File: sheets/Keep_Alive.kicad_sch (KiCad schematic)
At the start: 7 parts, among them IC1 PSM712-LF-T7, U41 MIC5205-3.3YM5

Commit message: Remediate power supply, main relay keep-alive, and schematic ERC to 0 errors
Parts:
- added D20, D21: B340A-13-F, Diode_SMD:D_SMA, symbol Device:D_Schottky
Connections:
- new net 12V_IGN_SW: D20.2 (A)
- new net 12V_MR: D21.2 (A)
- new net 12V_RAW: D20.1 (K), D21.1 (K)
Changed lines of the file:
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@@
+		)
+	)
+	(hierarchical_label "12V_IGN_SW"
+		(shape input)
+		(at 67.31 45.72 180)
+		(fields_autoplaced yes)
+		(effects (font (size 1.27 1.27)) (justify right))
+	)
+	(hierarchical_label "12V_MR"
+		(shape input)
+		(at 67.31 55.88 180)
+		(fields_autoplaced yes)
+		(effects (font (size 1.27 1.27)) (justify right))
+	)
+	(hierarchical_label "12V_RAW"
+		(shape output)
+		(at 120.65 45.72 0)
+		(fields_autoplaced yes)
+		(effects (font (size 1.27 1.27)) (justify left))
+	)
+	(wire
+		(pts (xy 67.31 45.72) (xy 86.36 45.72))
+		(stroke (width 0) (type default))
+	)
+	(wire
+		(pts (xy 67.31 55.88) (xy 86.36 55.88))
+		(stroke (width 0) (type default))
+	)
+	(wire
+		(pts (xy 93.98 45.72) (xy 105.41 45.72))
+		(stroke (width 0) (type default))
+	)
+	(wire
+		(pts (xy 93.98 55.88) (xy 105.41 55.88))
+		(stroke (width 0) (type default))
+	)
+	(wire
+		(pts (xy 105.41 55.88) (xy 105.41 45.72))
+		(stroke (width 0) (type default))
+	)
+	(wire
+		(pts (xy 105.41 45.72) (xy 120.65 45.72))
+		(stroke (width 0) (type default))
+	)
+	(junction
+		(at 105.41 45.72)
+		(diameter 0)
+		(color 0 0 0 0)
+	)
+	(symbol
+		(lib_id "Device:D_Schottky")
+		(at 90.17 45.72 180)
+		(unit 1)
+		(exclude_from_sim no)
+		(in_bom yes)
+		(on_board yes)
+		(dnp no)
+		(property "Reference" "D20"
+			(at 90.17 43.18 0)
+			(effects (font (size 1.27 1.27)))
+		)
+		(property "Value" "B340A-13-F"
+			(at 90.17 48.26 0)
+			(effects (font (size 1.27 1.27)))
+		)
+		(property "Footprint" "Diode_SMD:D_SMA"
+			(at 90.17 45.72 0)
+			(effects (font (size 1.27 1.27)) (hide yes))
+		)
+		(property "Datasheet" "~"
+			(at 90.17 45.72 0)
+			(effects (font (size 1.27 1.27)) (hide yes))
+		)
+		(property "Description" "40V 3A Schottky Barrier Diode (IGN_SW -> 12V_RAW OR-ing)"
+			(at 90.17 45.72 0)
+			(effects (font (size 1.27 1.27)) (hide yes))
+		)
+		(property "LCSC" "C8598"
+			(at 90.17 45.72 0)
+			(effects (font (size 1.27 1.27)) (hide yes))
+		)
+		(pin "1")
+		(pin "2")
+		(instances
+			(project "fome-mc"
+				(path "/3b9c5ffd-e59b-402d-8c5e-052f7ca643a4/46495fed-359e-4c30-808a-9217af090de7"
+					(reference "D20")
+					(unit 1)
+				)
+			)
+		)
+	)
+	(symbol
+		(lib_id "Device:D_Schottky")
+		(at 90.17 55.88 180)
+		(unit 1)
+		(exclude_from_sim no)
+		(in_bom yes)
+		(on_board yes)
+		(dnp no)
+		(property "Reference" "D21"
+			(at 90.17 53.34 0)
+			(effects (font (size 1.27 1.27)))
+		)
+		(property "Value" "B340A-13-F"
+			(at 90.17 58.42 0)
+			(effects (font (size 1.27 1.27)))
+		)
+		(property "Footprint" "Diode_SMD:D_SMA"
+			(at 90.17 55.88 0)
+			(effects (font (size 1.27 1.27)) (hide yes))
+		)
+		(property "Datasheet" "~"
+			(at 90.17 55.88 0)
+			(effects (font (size 1.27 1.27)) (hide yes))
+		)
+		(property "Description" "40V 3A Schottky Barrier Diode (12V_MR -> 12V_RAW Keep-Alive OR-ing)"
+			(at 90.17 55.88 0)
+			(effects (font (size 1.27 1.27)) (hide yes))
+		)
+		(property "LCSC" "C8598"
+			(at 90.17 55.88 0)
+			(effects (font (size 1.27 1.27)) (hide yes))
+		)
+		(pin "1")
+		(pin "2")
+		(instances
+			(project "fome-mc"
+				(path "/3b9c5ffd-e59b-402d-8c5e-052f7ca643a4/46495fed-359e-4c30-808a-9217af090de7"
+					(reference "D21")
+					(unit 1)
+				)
+			)
 		)
 	)

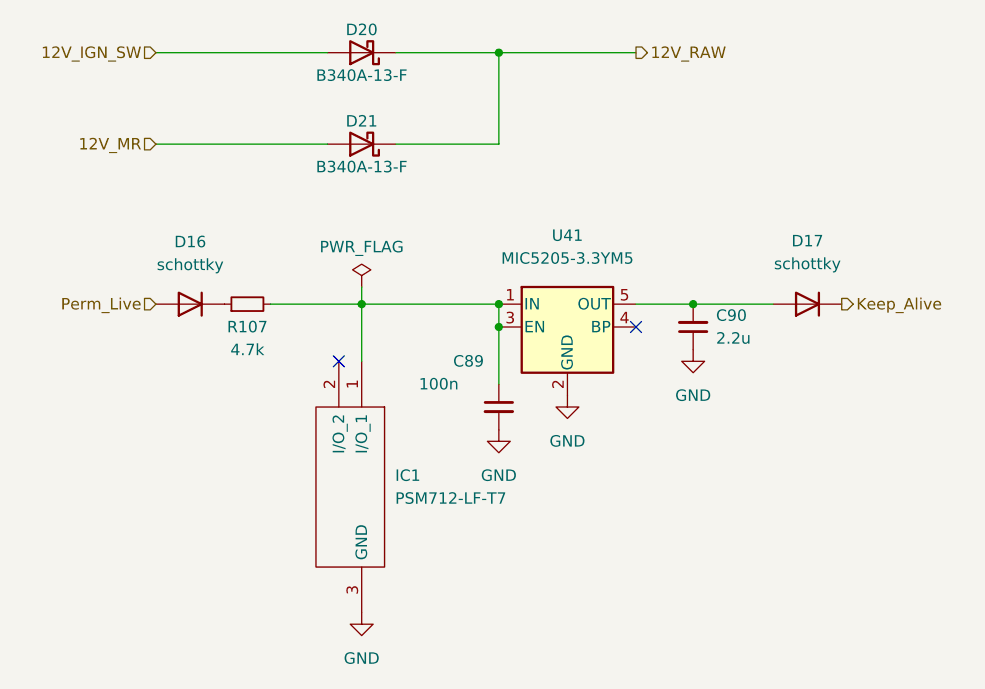
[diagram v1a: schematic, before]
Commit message: Add D210 BZT52C6V8 BOOT0 threshold Zener, R217/R218/D211 PA9 VBUS sense divider/clamp, and SMCJ24A TVS protection on 12V_RAW and 12V_MR (FOMEMC-7)
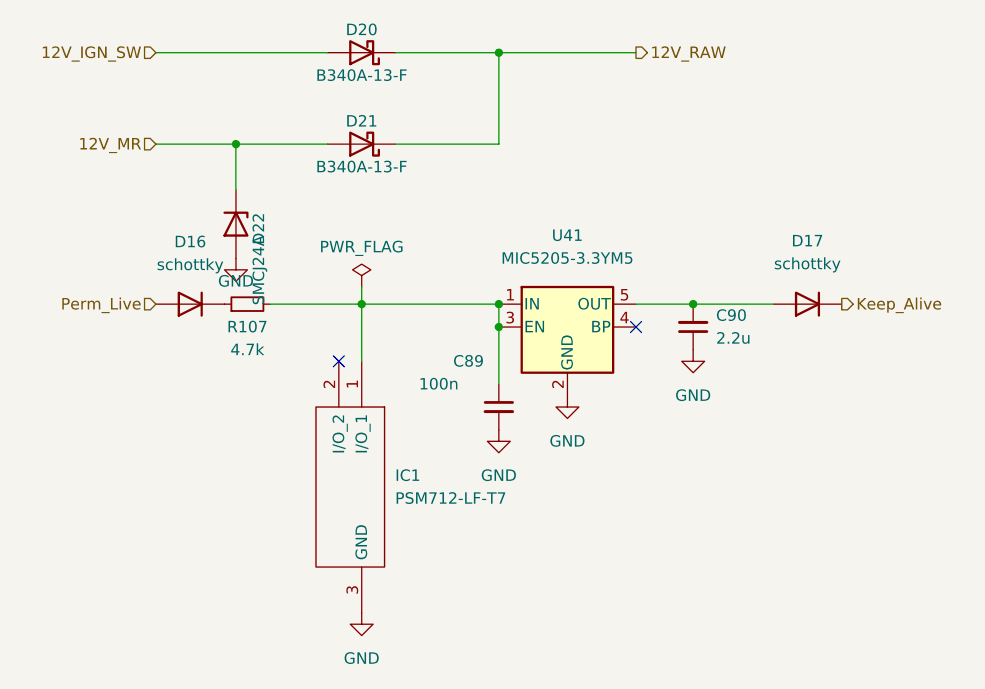
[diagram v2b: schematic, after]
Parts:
- added D22: SMCJ24A, Diode_SMD:D_SMC, symbol Device:D_Zener
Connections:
- net 12V_MR: now also D22.1 (K)
- net GND: now also D22.2 (A)
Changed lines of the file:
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@@
 	)
 	(wire
-		(pts (xy 67.31 55.88) (xy 86.36 55.88))
-		(stroke (width 0) (type default))
+		(pts (xy 67.31 55.88) (xy 76.2 55.88))
+		(stroke (width 0) (type default))
+	)
+	(wire
+		(pts (xy 76.2 55.88) (xy 86.36 55.88))
+		(stroke (width 0) (type default))
+	)
+	(wire
+		(pts (xy 76.2 55.88) (xy 76.2 60.96))
+		(stroke (width 0) (type default))
+	)
+	(junction
+		(at 76.2 55.88)
+		(diameter 0)
+		(color 0 0 0 0)
 	)
 	(wire
@@
 					(unit 1)
 				)
+			)
+		)
+	)
+	(symbol
+		(lib_id "Device:D_Zener")
+		(at 76.2 64.77 270)
+		(unit 1)
+		(exclude_from_sim no)
+		(in_bom yes)
+		(on_board yes)
+		(dnp no)
+		(property "Reference" "D22"
+			(at 78.74 63.5 0)
+			(effects (font (size 1.27 1.27)) (justify left))
+		)
+		(property "Value" "SMCJ24A"
+			(at 78.74 66.04 0)
+			(effects (font (size 1.27 1.27)) (justify left))
+		)
+		(property "Footprint" "Diode_SMD:D_SMC"
+			(at 76.2 64.77 0)
+			(effects (font (size 1.27 1.27)) (hide yes))
+		)
+		(property "Datasheet" "~"
+			(at 76.2 64.77 0)
+			(effects (font (size 1.27 1.27)) (hide yes))
+		)
+		(property "Description" "1500W 24V Unidirectional SMC TVS Diode on 12V_MR (38.9V max clamp)"
+			(at 76.2 64.77 0)
+			(effects (font (size 1.27 1.27)) (hide yes))
+		)
+		(property "PN" "SMCJ24A"
+			(at 76.2 64.77 0)
+			(effects (font (size 1.27 1.27)) (hide yes))
+		)
+		(property "LCSC" "C224045"
+			(at 76.2 64.77 0)
+			(effects (font (size 1.27 1.27)) (hide yes))
+		)
+		(pin "1")
+		(pin "2")
+		(instances
+			(project "fome-mc"
+				(path "/3b9c5ffd-e59b-402d-8c5e-052f7ca643a4/46495fed-359e-4c30-808a-9217af090de7"
+					(reference "D22")
+					(unit 1)
+				)
+			)
+		)
+	)
+	(symbol
+		(lib_id "power:GND")
+		(at 76.2 68.58 0)
+		(unit 1)
+		(exclude_from_sim no)
+		(in_bom yes)
+		(on_board yes)
+		(dnp no)
+		(property "Reference" "#PWR060"
+			(at 76.2 71.12 0)
+			(effects (font (size 1.27 1.27)) (hide yes))
+		)
+		(property "Value" "GND"
+			(at 76.2 71.12 0)
+			(effects (font (size 1.27 1.27)))
+		)
+		(property "Footprint" ""
+			(at 76.2 68.58 0)
+			(effects (font (size 1.27 1.27)) (hide yes))
+		)
+		(property "Datasheet" ""
+			(at 76.2 68.58 0)
+			(effects (font (size 1.27 1.27)) (hide yes))
+		)
+		(pin "1")
+		(instances
+			(project "fome-mc"
+				(path "/3b9c5ffd-e59b-402d-8c5e-052f7ca643a4/46495fed-359e-4c30-808a-9217af090de7"
+					(reference "#PWR060")
+					(unit 1)
+				)

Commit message: Add SDMMC1 47k pull-ups (R127..R131) & 22R clock damping (R132), mark U24 LPS25HB DNP, fix B340A/B5819W LCSC codes, and reconcile docs/verify_io_map (FOMEMC-8)
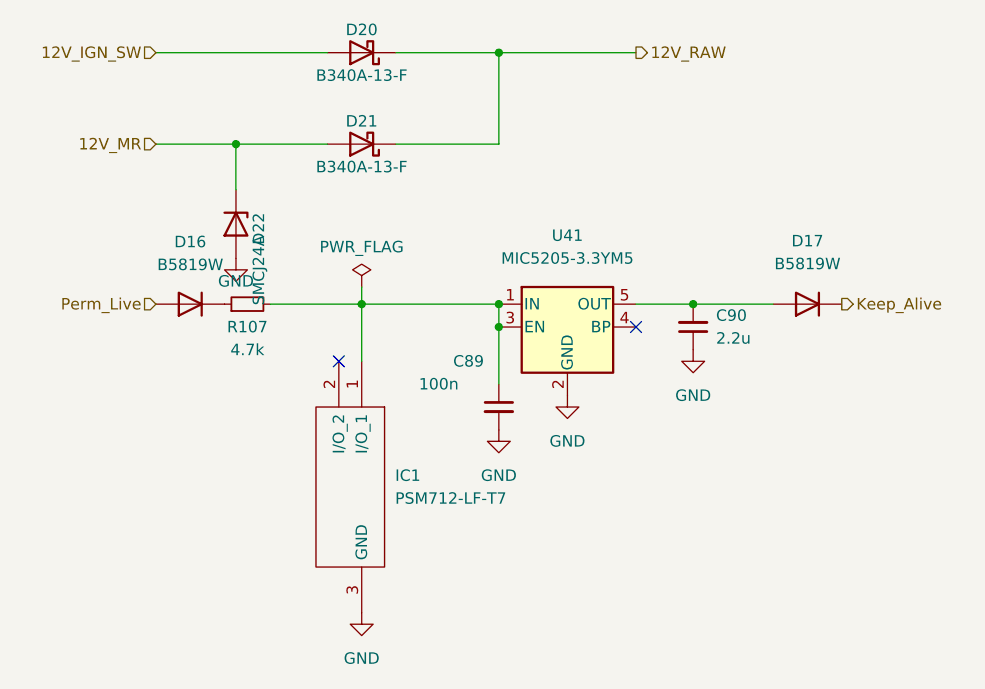
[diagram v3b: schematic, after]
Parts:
- D16, D17: value schottky -> B5819W
- D20, D21: LCSC C8598 -> C64982
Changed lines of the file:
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@@
 			)
 		)
-		(property "Value" "schottky"
+		(property "Value" "B5819W"
 			(at 139.7 69.1885 0)
 			(effects
@@
 			)
 		)
-		(property "Value" "schottky"
+		(property "Value" "B5819W"
 			(at 71.12 69.2882 0)
 			(effects
@@
 			(effects (font (size 1.27 1.27)) (hide yes))
 		)
-		(property "LCSC" "C8598"
+		(property "LCSC" "C64982"
 			(at 90.17 45.72 0)
 			(effects (font (size 1.27 1.27)) (hide yes))
@@
 			(effects (font (size 1.27 1.27)) (hide yes))
 		)
-		(property "LCSC" "C8598"
+		(property "LCSC" "C64982"
 			(at 90.17 55.88 0)
 			(effects (font (size 1.27 1.27)) (hide yes))

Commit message: Remediate FOMEMC-22..27: sheet contracts, doc/BOM/netlist parity, 494-part BOM/CPL, Mode A2 VR + C38/C39, wide WBO heater buses, and 4x M4 holes with 0 DRC warnings
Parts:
- C89: LCSC C14663 -> C161115
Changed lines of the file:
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@@
 			)
 		)
-		(property "LCSC" "C14663"
+		(property "LCSC" "C161115"
 			(at 105.41 85.09 0)
 			(effects
